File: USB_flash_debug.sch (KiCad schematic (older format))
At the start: 30 parts, among them IC2 TPS7A0518PDBVT, J10 WE_632723300011, J9 0473460001, Q7 BSS138-7-F, Q8 BSS138-7-F, SW1 1X03, U12 FSUSB30MUX, U13 FT232RQ-REEL

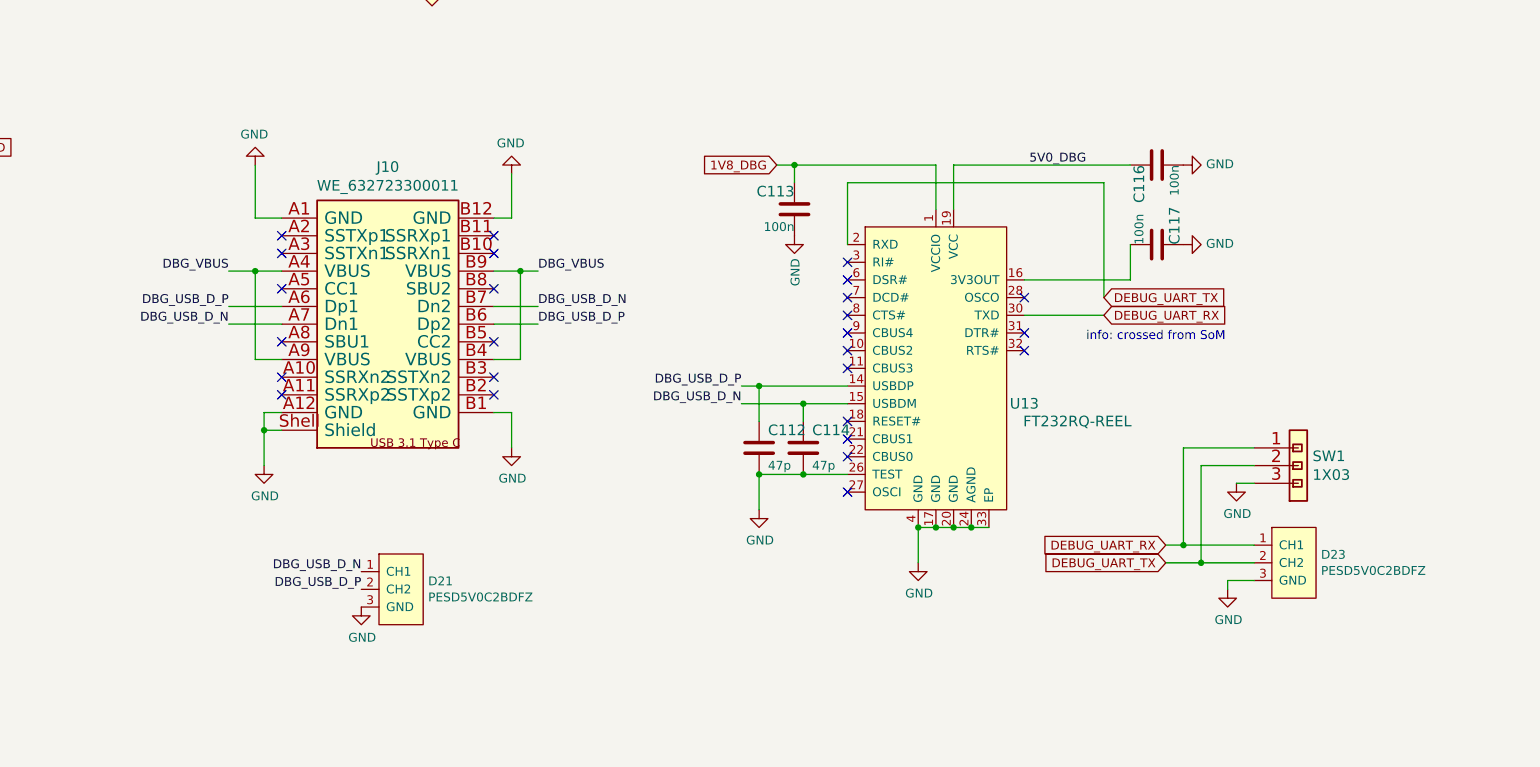
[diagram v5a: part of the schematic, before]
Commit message: USB Debug changed to micro USB. Started modifications on shortening board by 1cm
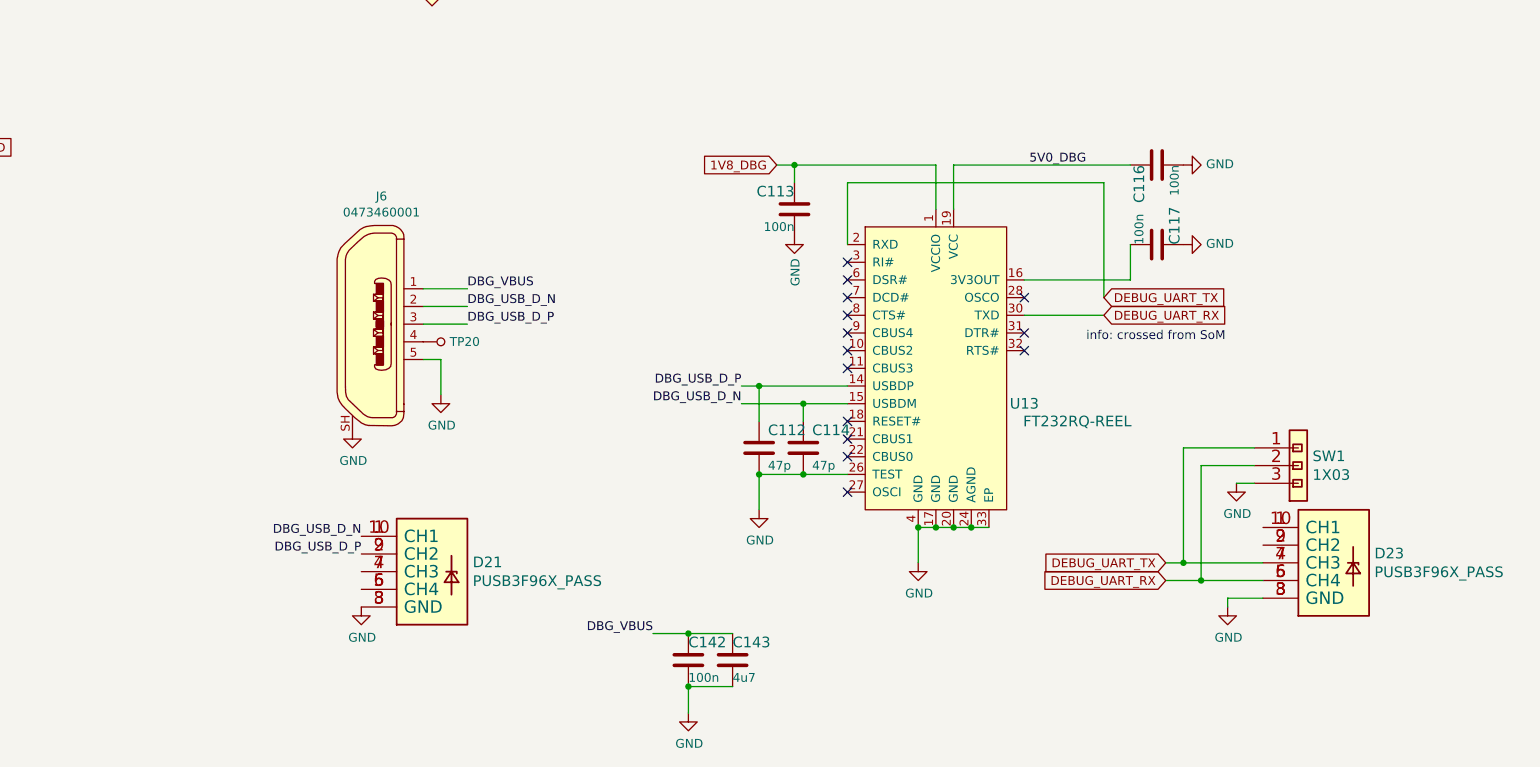
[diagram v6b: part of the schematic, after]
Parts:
- removed D21, D23: PESD5V0C2BDFZ, sc606-baseboard-footprints:DFN0603-3, symbol sc606-baseboard:PESD5V0C2BDFZ
- removed J10: WE_632723300011, sc606-baseboard-footprints:WE_632723300011, symbol sc606-baseboard:WE_632723300011
- added C142: C_100n_0402, sc606-baseboard-footprints:0402-cap, symbol sc606-baseboard:C_100n_0402
- added C143: C_4u7_0402, sc606-baseboard-footprints:0402-cap, symbol sc606-baseboard:C_4u7_0402
- added D21, D23: PUSB3F96X_PASS, sc606-baseboard-footprints:PUSB3F96X, symbol sc606-baseboard:PUSB3F96X_PASS
- added J6: 0473460001, sc606-baseboard-footprints:USB_Micro_B_Female_0473460001, symbol sc606-baseboard:0473460001
- added TP20: TP_SMD_0_75MM, sc606-baseboard-footprints:Testpoint_smd_0_75mm, symbol sc606-baseboard:TP_SMD_0_75MM
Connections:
- net DBG_USB_D_N: now also D21.1 (CH1), D21.10 (CH1), J6.2
- net DBG_USB_D_P: now also D21.2 (CH2), D21.9 (CH2), J6.3
- net DBG_VBUS: now also C142.1, C143.1, J6.1
- net DEBUG_UART_RX: now also SW1.2, D23.5 (CH4), D23.6 (CH4); no longer SW1.1
- net DEBUG_UART_TX: now also SW1.1, D23.4 (CH3), D23.7 (CH3); no longer SW1.2
- net GND: now also C142.2, C143.2, D21.3 (GND), D21.8 (GND), D23.3 (GND), D23.8 (GND), J6.5, J6.SH
- new net: J6.4, TP20.1
- new net: D21.4 (CH3), D21.7 (CH3)
- new net: D21.5 (CH4), D21.6 (CH4)
- new net: D23.1 (CH1), D23.10 (CH1)
- new net: D23.2 (CH2), D23.9 (CH2)
- no-connect marks 26 -> 14

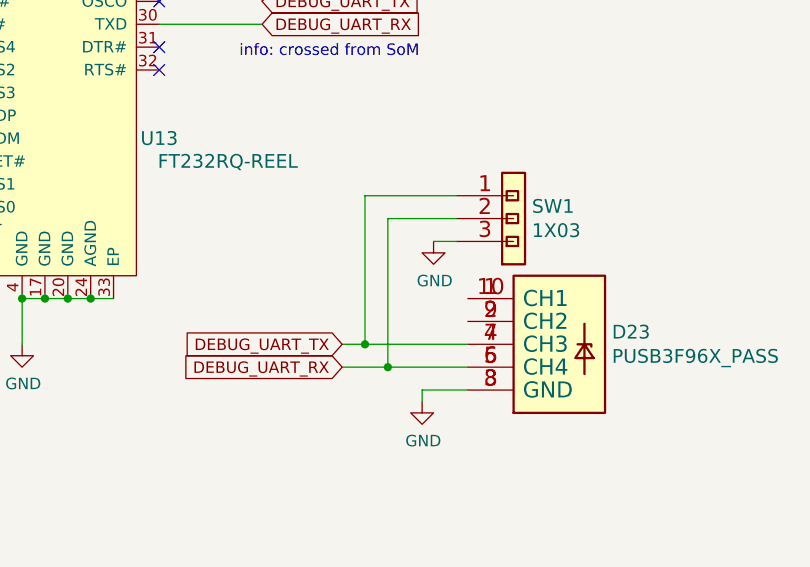
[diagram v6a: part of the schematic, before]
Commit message: Finished placement after shortening board by 1cm
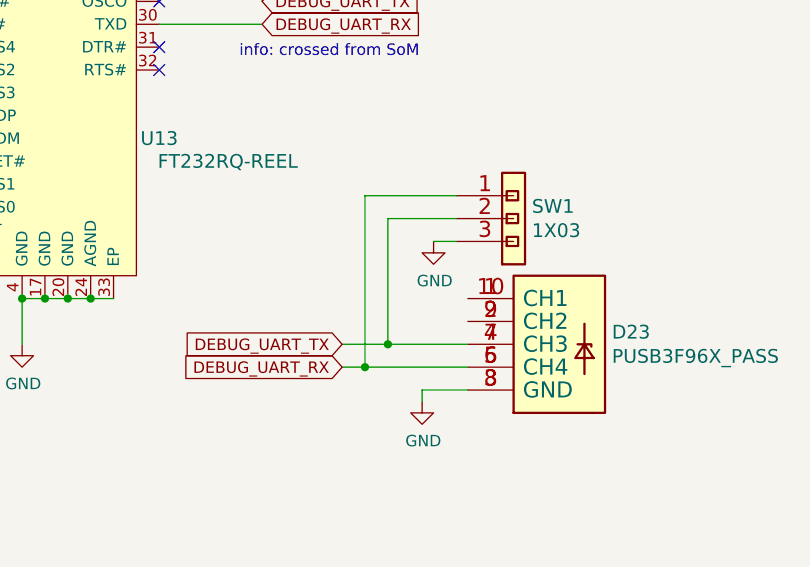
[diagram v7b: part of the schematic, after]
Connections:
- net DEBUG_UART_RX: now also SW1.1; no longer SW1.2
- net DEBUG_UART_TX: now also SW1.2; no longer SW1.1
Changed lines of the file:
@@
 $EndComp
 Wire Wire Line
-	14250 5400 14350 5400
+	14250 5400 14450 5400
 Wire Wire Line
-	14350 5400 14800 5400
-Connection ~ 14350 5400
+	14250 5500 14350 5500
 Wire Wire Line
-	14350 4750 14350 5400
+	14450 4850 14450 5400
+Connection ~ 14450 5400
 Wire Wire Line
-	14250 5500 14450 5500
+	14450 5400 14800 5400
 Wire Wire Line
-	14450 5500 14800 5500
-Connection ~ 14450 5500
+	14350 4750 14350 5500
+Connection ~ 14350 5500
 Wire Wire Line
-	14450 4850 14450 5500
+	14350 5500 14800 5500
 $EndSCHEMATC

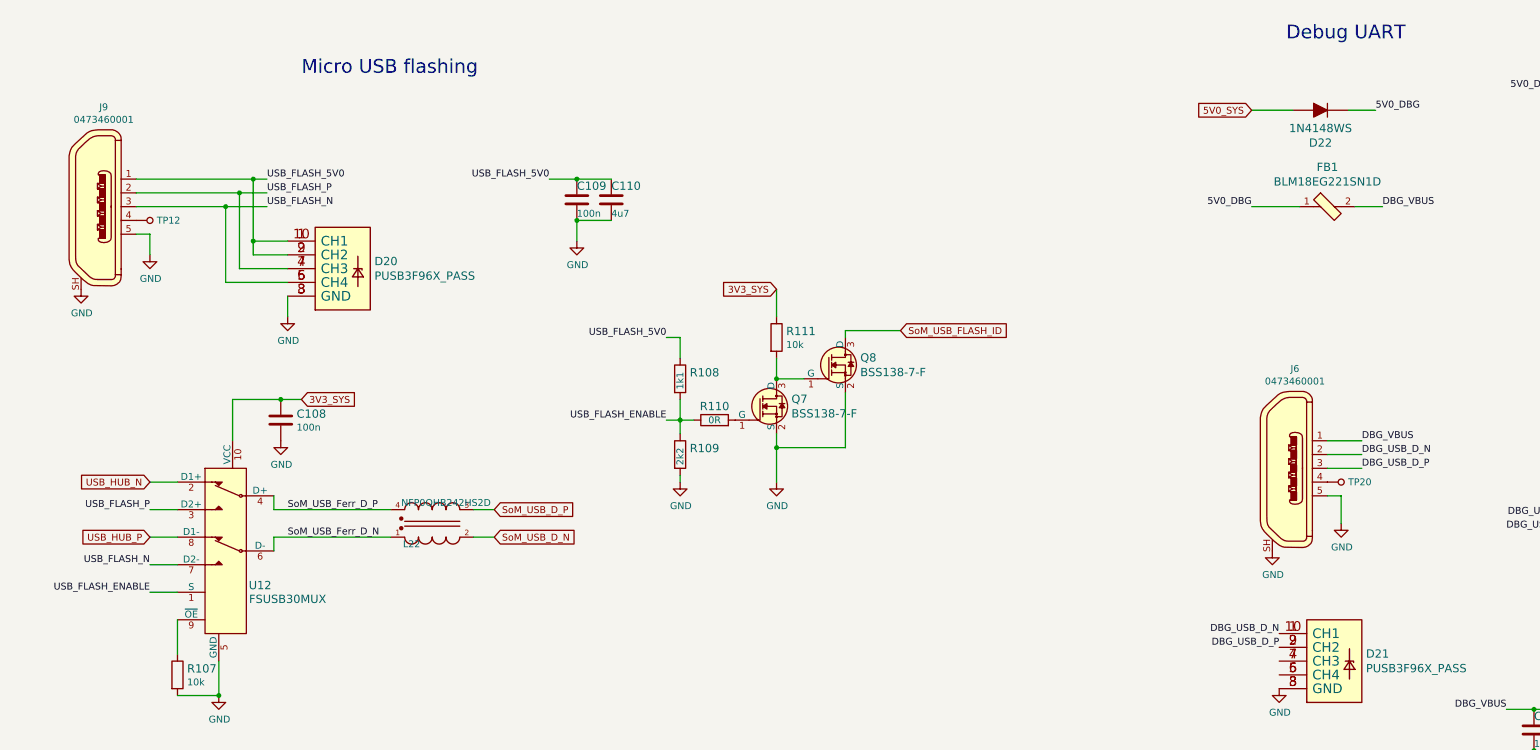
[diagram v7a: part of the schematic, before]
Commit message: Changed USB flash and debug to USB-C. Prepared place for USB PD. Minor modifications of components position
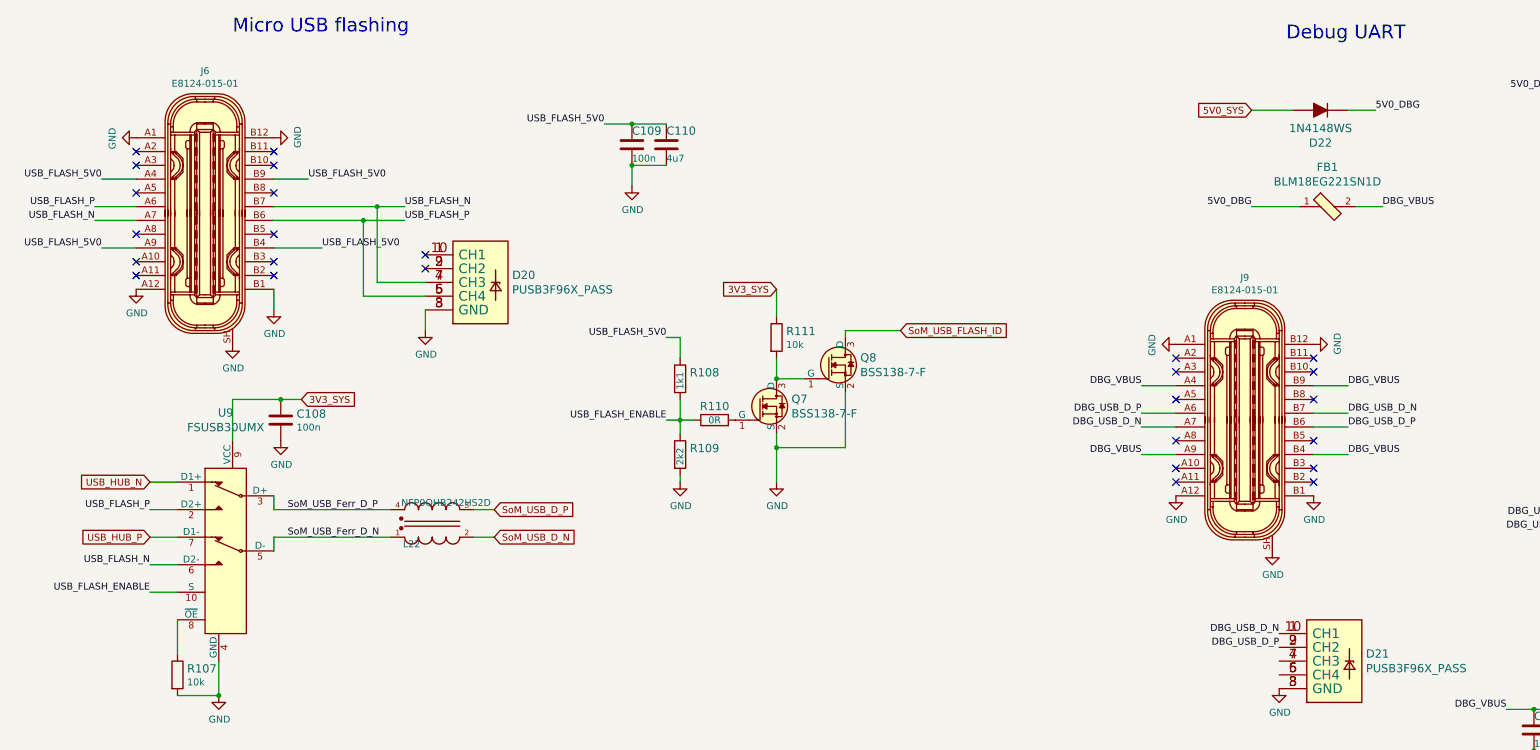
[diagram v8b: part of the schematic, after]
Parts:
- removed J6, J9: 0473460001, sc606-baseboard-footprints:USB_Micro_B_Female_0473460001, symbol sc606-baseboard:0473460001
- removed TP12, TP20: TP_SMD_0_75MM, sc606-baseboard-footprints:Testpoint_smd_0_75mm, symbol sc606-baseboard:TP_SMD_0_75MM
- removed U12: FSUSB30MUX, sc606-baseboard-footprints:MSOP-10_W3mm, symbol sc606-baseboard:FSUSB30MUX
- added J6, J9: E8124-015-01, sc606-baseboard-footprints:USB-C_Female_E8124-015-01, symbol sc606-baseboard:E8124-015-01
- added U9: FSUSB30UMX, sc606-baseboard-footprints:UMLP-10_1.8x1.4mm, symbol sc606-baseboard:FSUSB30UMX
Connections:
- net 3V3_SYS: now also U9.9 (VCC)
- net DBG_USB_D_N: now also J9.A7, J9.B7
- net DBG_USB_D_P: now also J9.A6, J9.B6
- net DBG_VBUS: now also J9.A4, J9.A9, J9.B4, J9.B9
- net GND: now also J6.A1, J6.A12, J6.B1, J6.B12, J6.SH, J9.A1, J9.A12, J9.B1, J9.B12, J9.SH, U9.4 (GND)
- net SoM_USB_Ferr_D_N: now also U9.5 (D-)
- net SoM_USB_Ferr_D_P: now also U9.3 (D+)
- net USB_FLASH_5V0: now also J6.A4, J6.A9, J6.B4, J6.B9; no longer D20.1 (CH1), D20.10 (CH1), D20.2 (CH2), D20.9 (CH2)
- net USB_FLASH_ENABLE: now also U9.10 (S)
- net USB_FLASH_N: now also D20.4 (CH3), D20.7 (CH3), J6.A7, J6.B7, U9.6 (D2-); no longer D20.5 (CH4), D20.6 (CH4)
- net USB_FLASH_P: now also D20.5 (CH4), D20.6 (CH4), J6.A6, J6.B6, U9.2 (D2+); no longer D20.4 (CH3), D20.7 (CH3)
- net USB_HUB_N: now also U9.1 (D1+)
- net USB_HUB_P: now also U9.7 (D1-)
- net at R107.1: now also U9.8 (~OE)
- new net: D20.1 (CH1), D20.10 (CH1)
- new net: D20.2 (CH2), D20.9 (CH2)
- no-connect marks 14 -> 40
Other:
- moved on the sheet: C109, C110, D20
